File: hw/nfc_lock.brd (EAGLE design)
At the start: 100 x 80 mm, 14 parts, among them IC1 STM8S003F3, IC3 MCP170312MB, U1 M24SR16-YMN6T/2, U2 IRFML8244TRPBF, U3 IRFML8244TRPBF, X1 MINI-USB-32005-301

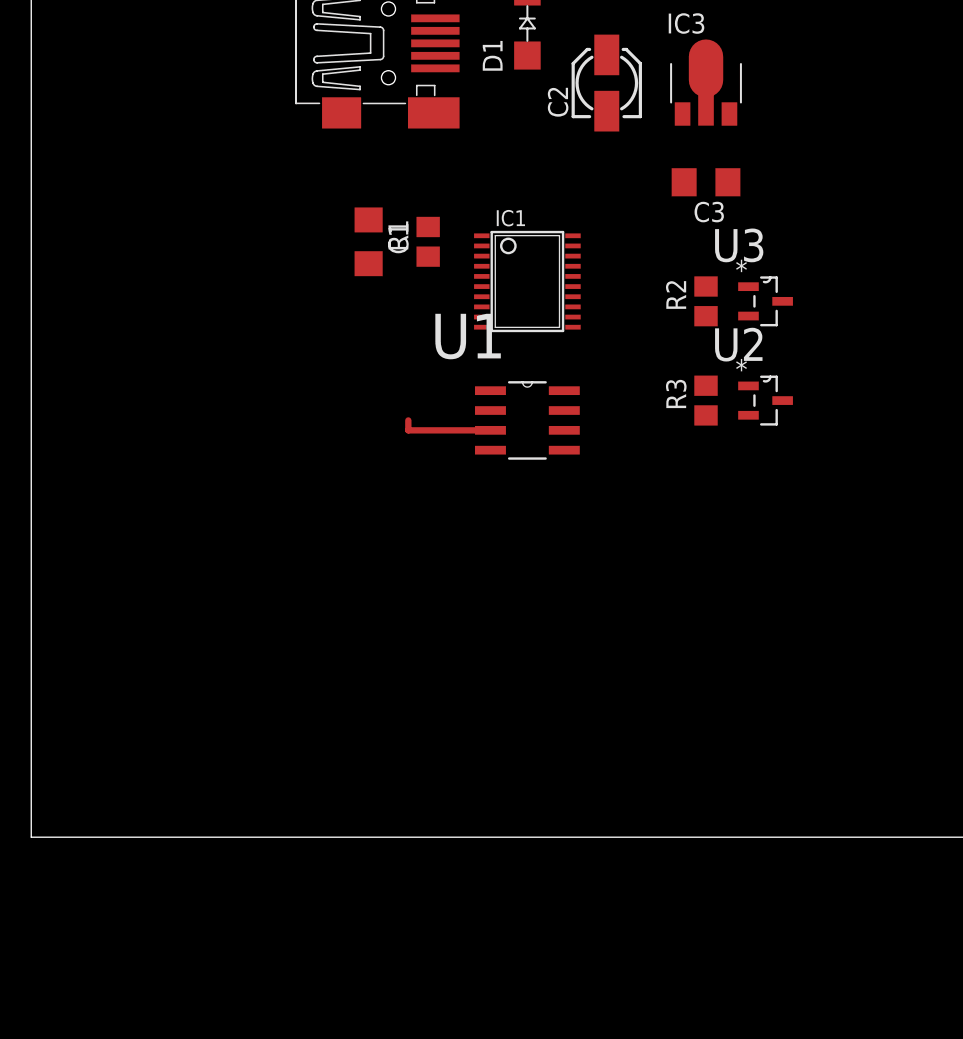
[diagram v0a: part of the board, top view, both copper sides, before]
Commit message: added SWIM, connections to servos, signalling LED
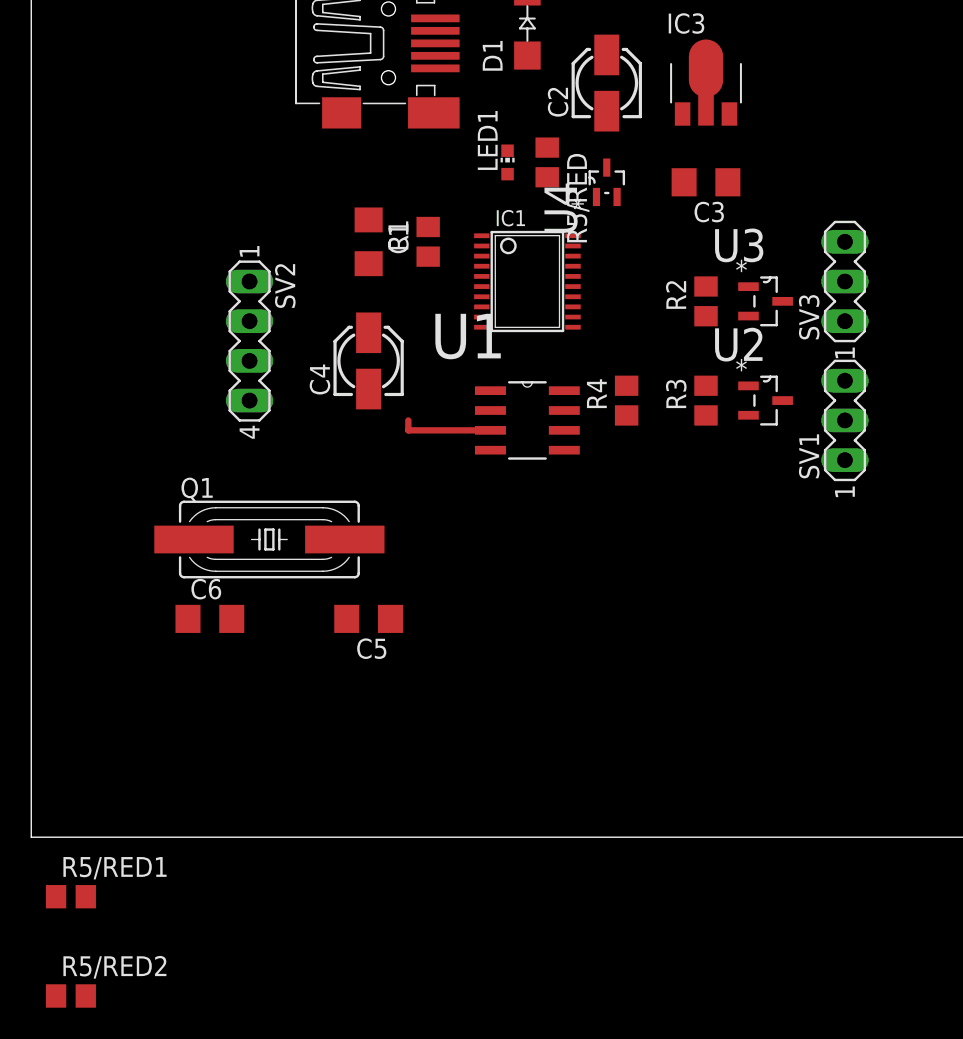
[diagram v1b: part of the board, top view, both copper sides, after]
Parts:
- added C4: 1uF, rcl:153CLV-0405
- added C5, C6: 33pF, rcl:C1206
- added LED1: (no value), led:CHIP-LED0603
- added Q1: 8MHz, crystal:SM49
- added R4, R5/RED2: 10k, rcl:R0805
- added R5/RED: 470R, rcl:R0805
- added R5/RED1: 24k, rcl:R0805
- added SV1: SERVO#1, con-lstb:MA03-1
- added SV2: SWIM, con-lstb:MA04-1
- added SV3: SERVO#2, con-lstb:MA03-1
- added U4: 2N7002BKW, 2n7002:SOT65P210X110-3N
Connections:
- net N$10 renamed ANTENA
- removed net VCAP: IC1.8
- new net N$11: SV3.2, U3.3
- new net N$12: LED1.C, R5/RED.1
- new net N$14: R5/RED.2, U4.3
- new net N$15: C4.+, IC1.8
- new net N$16: C5.2, IC1.5, Q1.2
- new net N$17: C6.1, IC1.6, Q1.1
- new net N$18: IC1.19, R5/RED1.2, R5/RED2.1
- new net N$19: IC1.16, U4.1
- new net N$9: SV1.2, U2.3
- net +5V/1: now also R4.2
- net +5V/2: now also LED1.A, R5/RED1.1, SV1.3, SV2.4, SV3.3
- net 0V: now also C4.-, C5.1, C6.2, R5/RED2.2, SV1.1, SV2.2, SV3.1, U4.2
- net N$5: now also SV2.1
- net N$6: now also SV2.3
- net N$8: now also R4.1

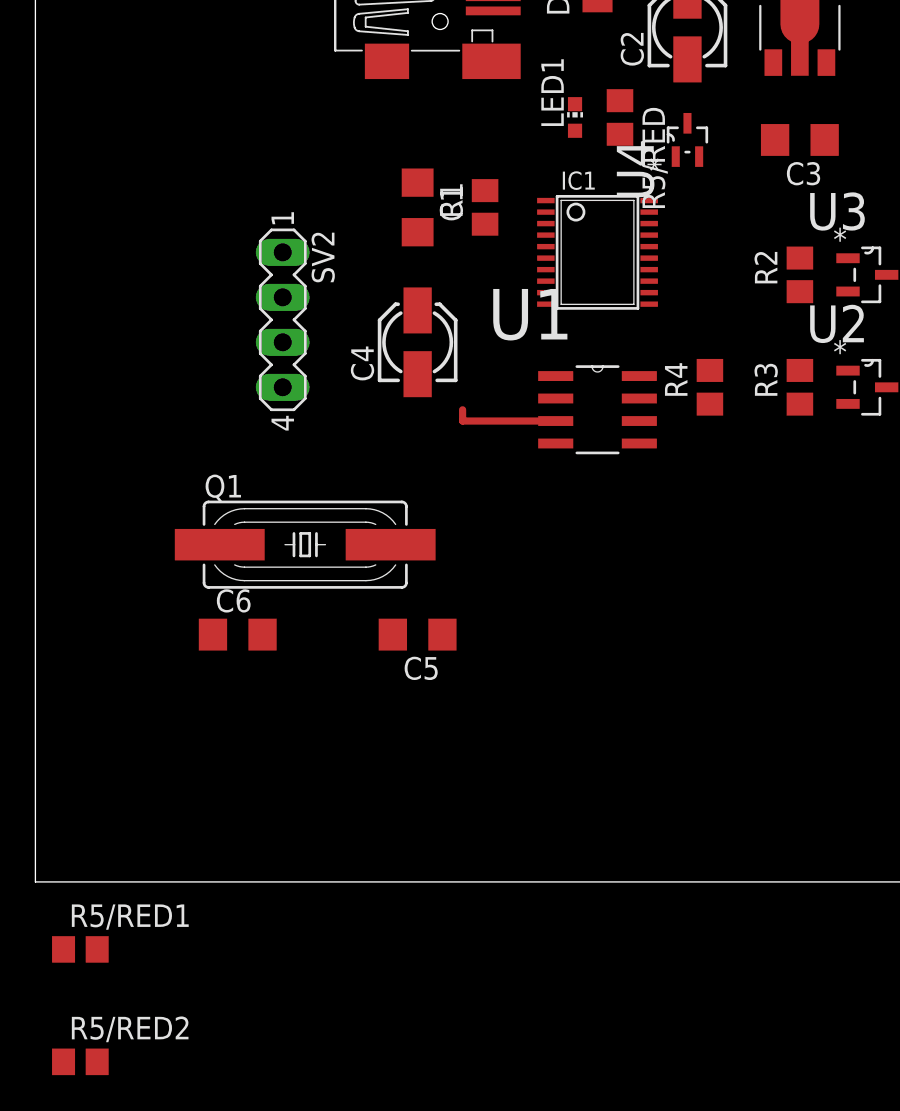
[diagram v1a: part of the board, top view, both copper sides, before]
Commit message: resistors not LEDs for voltage split
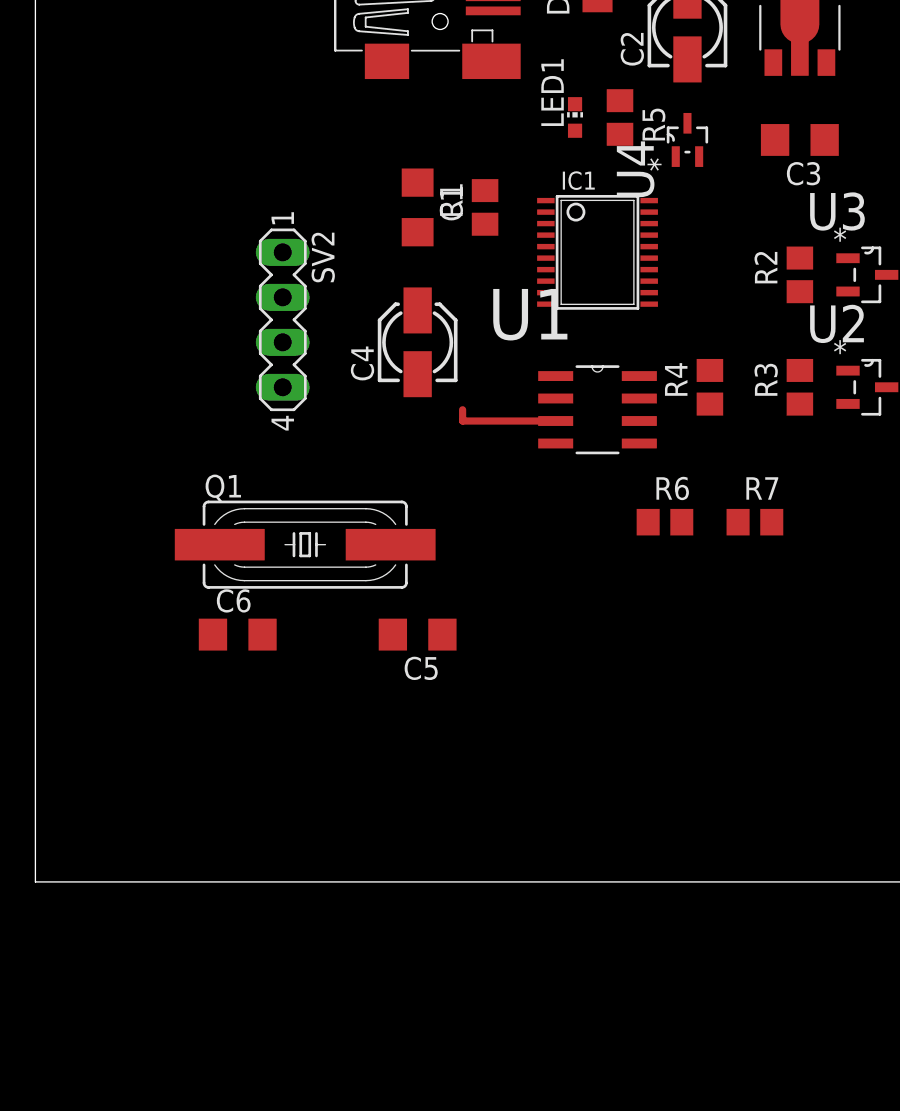
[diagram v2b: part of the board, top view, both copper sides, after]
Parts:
- removed R5/RED1: 24k, rcl:R0805
- removed R5/RED2: 10k, rcl:R0805
- added R6: 24k, rcl:R0805
- added R7: 10k, rcl:R0805
- LED1: value (none) -> RED
- renumbered R5/RED to R5
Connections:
- net +5V/2: now also R6.1; no longer R5/RED1.1
- net 0V: now also R7.2; no longer R5/RED2.2
- net N$18: now also R6.2, R7.1; no longer R5/RED1.2, R5/RED2.1
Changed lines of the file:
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@@
 <attribute name="MPN" value="2N7002BKW" x="36.83" y="41.91" size="1.778" layer="27" rot="R90" display="off"/>
 </element>
-<element name="LED1" library="led" package="CHIP-LED0603" value="" x="30.48" y="43.18"/>
-<element name="R5/RED" library="rcl" package="R0805" value="470R" x="33.02" y="43.18" rot="R270"/>
+<element name="LED1" library="led" package="CHIP-LED0603" value="RED" x="30.48" y="43.18"/>
+<element name="R5" library="rcl" package="R0805" value="470R" x="33.02" y="43.18" rot="R270"/>
 <element name="C4" library="rcl" package="153CLV-0405" value="1uF" x="21.59" y="30.48" rot="R90"/>
 <element name="Q1" library="crystal" package="SM49" value="8MHz" x="15.24" y="19.05">
@@
 <element name="C5" library="rcl" package="C1206" value="33pF" x="21.59" y="13.97" rot="R180"/>
 <element name="C6" library="rcl" package="C1206" value="33pF" x="11.43" y="13.97"/>
-<element name="R5/RED1" library="rcl" package="R0805" value="24k" x="2.54" y="-3.81"/>
-<element name="R5/RED2" library="rcl" package="R0805" value="10k" x="2.54" y="-10.16"/>
+<element name="R6" library="rcl" package="R0805" value="24k" x="35.56" y="20.32"/>
+<element name="R7" library="rcl" package="R0805" value="10k" x="40.64" y="20.32"/>
 </elements>
 <signals>
@@
 <contactref element="C5" pad="1"/>
 <contactref element="C6" pad="2"/>
-<contactref element="R5/RED2" pad="2"/>
+<contactref element="R7" pad="2"/>
 <wire x1="41.78" y1="41.91" x2="41.681" y2="46.279" width="0" layer="19" extent="1-1"/>
 <wire x1="37.4904" y1="40.9702" x2="41.78" y2="41.91" width="0" layer="19" extent="1-1"/>
@@
 <wire x1="43.18" y1="26.99" x2="45.8978" y2="27.0002" width="0" layer="19" extent="1-1"/>
 <wire x1="52.07" y1="24.13" x2="45.8978" y2="27.0002" width="0" layer="19" extent="1-1"/>
+<wire x1="41.59" y1="20.32" x2="43.18" y2="26.99" width="0" layer="19" extent="1-1"/>
 <wire x1="28.8322" y1="34.585" x2="37.4904" y2="40.9702" width="0" layer="19" extent="1-1"/>
 <wire x1="21.59" y1="36.7" x2="28.8322" y2="34.585" width="0" layer="19" extent="1-1"/>
@@
 <wire x1="22.99" y1="13.97" x2="29.3878" y2="24.765" width="0" layer="19" extent="1-1"/>
 <wire x1="12.83" y1="13.97" x2="22.99" y2="13.97" width="0" layer="19" extent="1-1"/>
-<wire x1="3.49" y1="-10.16" x2="12.83" y2="13.97" width="0" layer="19" extent="1-1"/>
 </signal>
 <signal name="+5V/1">
@@
 <contactref element="SV2" pad="4"/>
 <contactref element="LED1" pad="A"/>
-<contactref element="R5/RED1" pad="1"/>
+<contactref element="R6" pad="1"/>
 <wire x1="31.75" y1="54.12" x2="39.86" y2="54.61" width="0" layer="19" extent="1-1"/>
 <wire x1="30.48" y1="42.43" x2="31.75" y2="54.12" width="0" layer="19" extent="1-1"/>
 <wire x1="52.07" y1="38.1" x2="39.86" y2="54.61" width="0" layer="19" extent="1-1"/>
 <wire x1="52.07" y1="29.21" x2="52.07" y2="38.1" width="0" layer="19" extent="1-1"/>
+<wire x1="34.61" y1="20.32" x2="52.07" y2="29.21" width="0" layer="19" extent="1-1"/>
 <wire x1="13.97" y1="27.94" x2="30.48" y2="42.43" width="0" layer="19" extent="1-1"/>
-<wire x1="1.59" y1="-3.81" x2="13.97" y2="27.94" width="0" layer="19" extent="1-1"/>
 </signal>
 <signal name="N$3">
@@
 <signal name="N$12">
 <contactref element="LED1" pad="C"/>
-<contactref element="R5/RED" pad="1"/>
+<contactref element="R5" pad="1"/>
 <wire x1="30.48" y1="43.93" x2="33.02" y2="44.13" width="0" layer="19" extent="1-1"/>
 </signal>
 <signal name="N$14">
-<contactref element="R5/RED" pad="2"/>
+<contactref element="R5" pad="2"/>
 <contactref element="U4" pad="3"/>
 <wire x1="33.02" y1="42.23" x2="36.83" y2="42.8498" width="0" layer="19" extent="1-1"/>
@@
 <signal name="N$18">
 <contactref element="IC1" pad="19"/>
-<contactref element="R5/RED1" pad="2"/>
-<contactref element="R5/RED2" pad="1"/>
-<wire x1="3.49" y1="-3.81" x2="34.6678" y2="37.835" width="0" layer="19" extent="1-1"/>
-<wire x1="1.59" y1="-10.16" x2="3.49" y2="-3.81" width="0" layer="19" extent="1-1"/>
+<contactref element="R6" pad="2"/>
+<contactref element="R7" pad="1"/>
+<wire x1="36.51" y1="20.32" x2="34.6678" y2="37.835" width="0" layer="19" extent="1-1"/>
+<wire x1="39.69" y1="20.32" x2="36.51" y2="20.32" width="0" layer="19" extent="1-1"/>
 </signal>
 <signal name="N$19">

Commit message: antenna drawed
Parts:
- added R8: 30k, rcl:R0805
- R4: value 10k -> 20k
- moved C5 76.5 mm to (78.7, 64.8)
- moved C6 76.5 mm to (68.6, 64.8)
- moved Q1 76.5 mm to (72.4, 69.8)
- moved D2 20.7 mm to (38.1, 74.9)
- moved X1 20.7 mm to (19.1, 71.1)
- moved C1 20.7 mm to (17.8, 58.4)
- moved C2 20.7 mm to (33.0, 68.6)
- moved C3 20.7 mm to (39.4, 62.2)
- moved D1 20.7 mm to (27.9, 72.4)
- moved IC1 20.7 mm to (27.9, 55.9)
- moved IC3 20.7 mm to (39.4, 68.6)
- moved LED1 20.7 mm to (26.7, 63.5)
- moved R1 20.7 mm to (21.6, 58.4)
- moved R2 20.7 mm to (39.4, 54.6)
- moved R5 20.7 mm to (29.2, 63.5)
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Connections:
- net +5V/1: now also R8.2
- net N$7: now also R8.1
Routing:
- net ANTENA: track 5.89 -> 750.5 mm, vias 0 -> 2

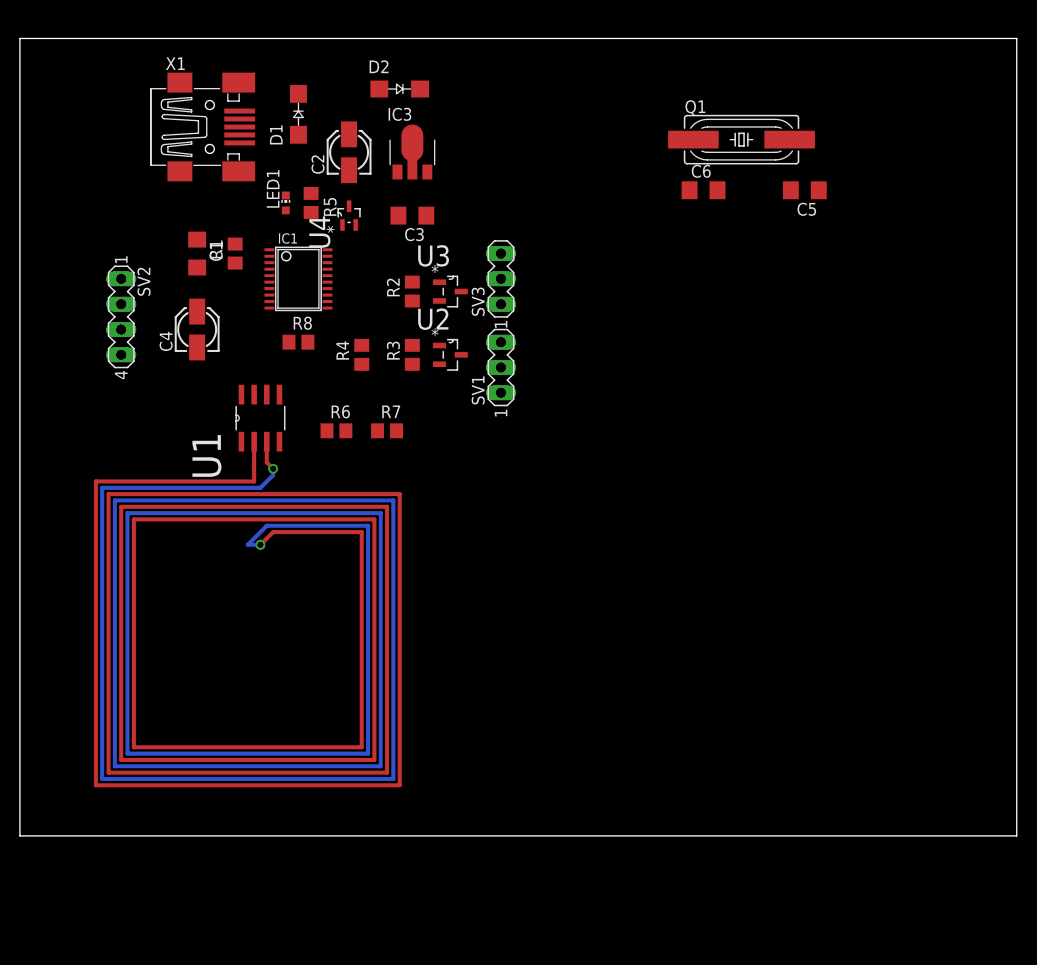
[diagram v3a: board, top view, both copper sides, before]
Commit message: added 2x more servos + some elements positioning
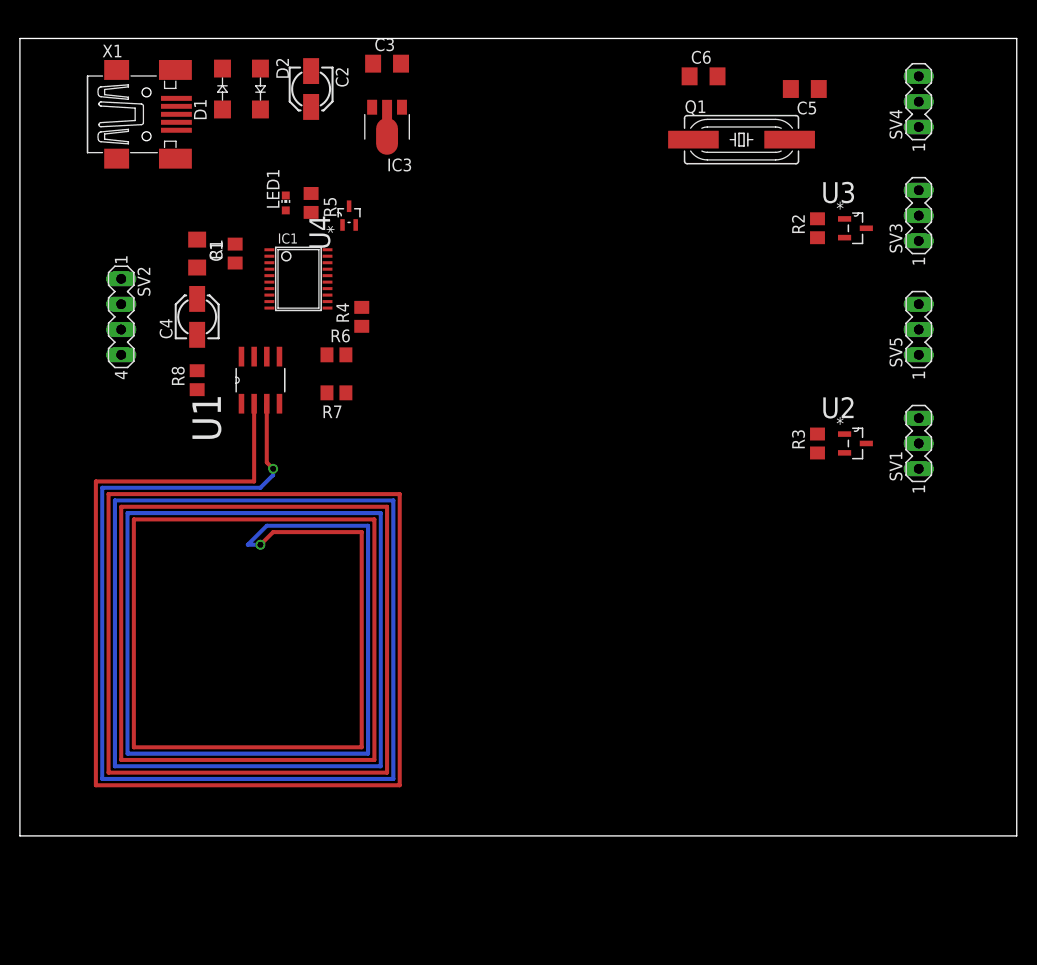
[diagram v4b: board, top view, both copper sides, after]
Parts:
- added SV4: SERVO#4, con-lstb:MA03-1
- added SV5: SERVO#2, con-lstb:MA03-1
- SV3: value SERVO#2 -> SERVO#3
- moved SV1 42.6 mm to (90.2, 39.4)
- moved SV3 42.4 mm to (90.2, 62.2)
- moved R3 41.6 mm to (80.0, 39.4)
- moved U2 41.6 mm to (83.8, 39.4)
- moved R2 41.1 mm to (80.0, 61.0)
- moved U3 41.1 mm to (83.8, 61.0)
- moved C3 15.5 mm to (36.8, 77.5), turned to 0 degrees
- moved D2 14.0 mm to (24.1, 74.9), turned to 270 degrees
- moved C6 11.4 mm to (68.6, 76.2)
- moved R8 10.9 mm to (17.8, 45.7), turned to 90 degrees
- moved C5 10.2 mm to (78.7, 74.9)
- moved D1 8.03 mm to (20.3, 74.9)
- moved R6 7.62 mm to (31.8, 48.3)
- moved C2 7.41 mm to (29.2, 74.9), turned to 270 degrees
- moved X1 6.48 mm to (12.7, 72.4)
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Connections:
- net +5V/2: now also SV4.3, SV5.3
- net 0V: now also SV4.1, SV5.1
- net N$11: now also SV4.2
- net N$9: now also SV5.2
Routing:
- net ANTENA: track 750.5 -> 758.1 mm
